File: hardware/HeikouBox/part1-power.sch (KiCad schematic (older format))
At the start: 20 parts, among them J101 5V, U101 LD1117S33TR, U102 LD1117S25TR, U103 LD1117S12TR

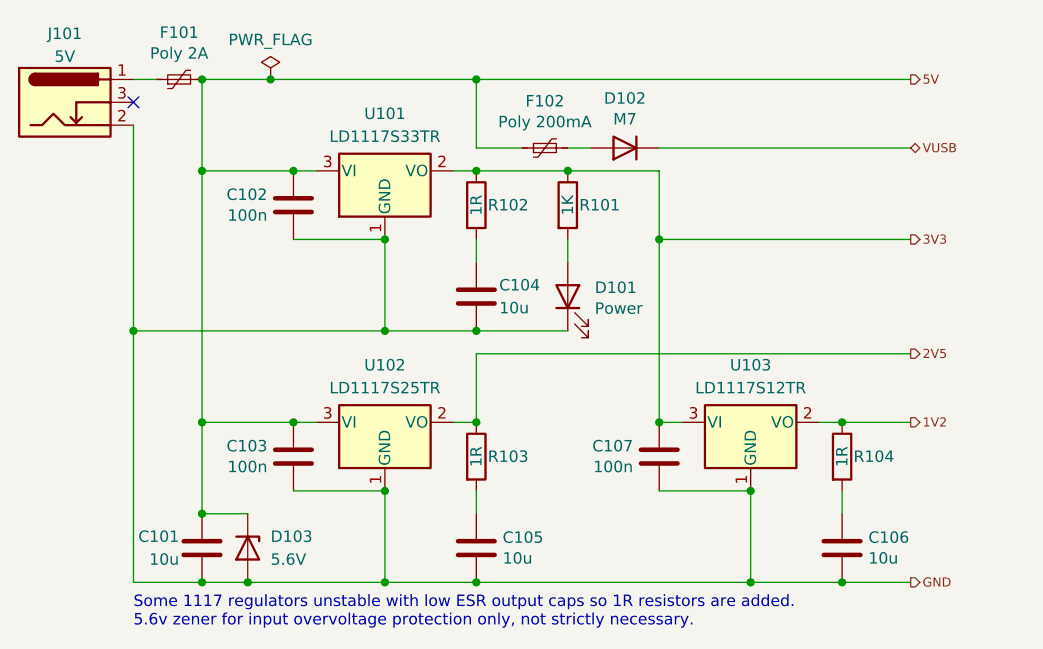
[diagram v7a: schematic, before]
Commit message: Update regulator capacitor values
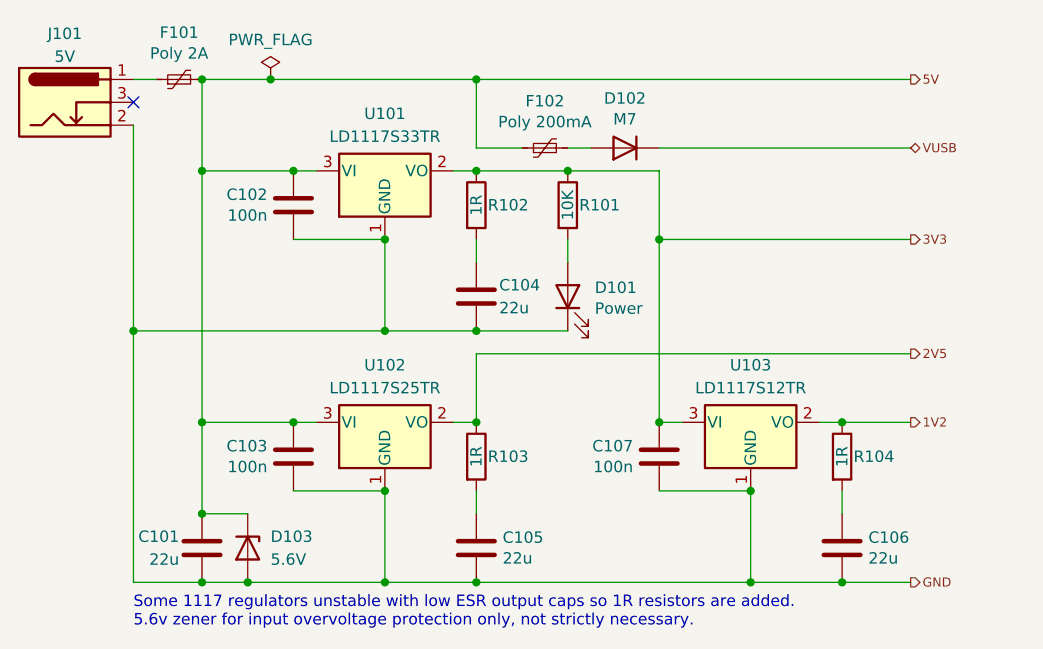
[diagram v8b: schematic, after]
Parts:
- C101, C104, C105, C106: value 10u -> 22u
- R101: value 1K -> 10K
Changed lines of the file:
@@
 	4200 2600 4200 2700
-$Comp
-L Device:R R?
-U 1 1 63836B0F
-P 2600 2450
-AR Path="/63836B0F" Ref="R?"  Part="1"
-AR Path="/644CBAED/63836B0F" Ref="R103"  Part="1"
-AR Path="/729F86A7/63836B0F" Ref="R?"  Part="1"
-F 0 "R103" H 2650 2450 50  0000 L CNN
-F 1 "1R" V 2600 2450 50  0000 C CNN
-F 2 "Resistor_SMD:R_0805_2012Metric_Pad1.20x1.40mm_HandSolder" V 2530 2450 50  0001 C CNN
-F 3 "~" H 2600 2450 50  0001 C CNN
-	1    2600 2450
-	1    0    0    -1
-$EndComp
 $Comp
 L Device:C C?
@@
 AR Path="/729F86A7/67C00E15" Ref="C?"  Part="1"
 F 0 "C106" H 4315 2896 50  0000 L CNN
-F 1 "10u" H 4315 2805 50  0000 L CNN
+F 1 "22u" H 4315 2805 50  0000 L CNN
 F 2 "Capacitor_SMD:C_0805_2012Metric_Pad1.18x1.45mm_HandSolder" H 4238 2700 50  0001 C CNN
 F 3 "~" H 4200 2850 50  0001 C CNN
@@
 AR Path="/729F86A7/67C00DA5" Ref="R?"  Part="1"
 F 0 "R101" H 3050 1350 50  0000 L CNN
-F 1 "1K" V 3000 1350 50  0000 C CNN
+F 1 "10K" V 3000 1350 50  0000 C CNN
 F 2 "Resistor_SMD:R_0603_1608Metric_Pad0.98x0.95mm_HandSolder" V 2930 1350 50  0001 C CNN
 F 3 "~" H 3000 1350 50  0001 C CNN
@@
 AR Path="/729F86A7/67C00E04" Ref="C?"  Part="1"
 F 0 "C105" H 2715 2896 50  0000 L CNN
-F 1 "10u" H 2715 2805 50  0000 L CNN
+F 1 "22u" H 2715 2805 50  0000 L CNN
 F 2 "Capacitor_SMD:C_0805_2012Metric_Pad1.18x1.45mm_HandSolder" H 2638 2700 50  0001 C CNN
 F 3 "~" H 2600 2850 50  0001 C CNN
@@
 AR Path="/729F86A7/67C00DAB" Ref="C?"  Part="1"
 F 0 "C104" H 2700 1800 50  0000 L CNN
-F 1 "10u" H 2700 1700 50  0000 L CNN
+F 1 "22u" H 2700 1700 50  0000 L CNN
 F 2 "Capacitor_SMD:C_0805_2012Metric_Pad1.18x1.45mm_HandSolder" H 2638 1600 50  0001 C CNN
 F 3 "~" H 2600 1750 50  0001 C CNN
@@
 AR Path="/729F86A7/67C00DB6" Ref="C?"  Part="1"
 F 0 "C101" H 1300 2900 50  0000 R CNN
-F 1 "10u" H 1300 2800 50  0000 R CNN
+F 1 "22u" H 1300 2800 50  0000 R CNN
 F 2 "Capacitor_SMD:C_0805_2012Metric_Pad1.18x1.45mm_HandSolder" H 1438 2700 50  0001 C CNN
 F 3 "~" H 1400 2850 50  0001 C CNN
@@
 Wire Wire Line
 	3400 1500 3400 1200
+$Comp
+L Device:R R?
+U 1 1 63836B0F
+P 2600 2450
+AR Path="/63836B0F" Ref="R?"  Part="1"
+AR Path="/644CBAED/63836B0F" Ref="R103"  Part="1"
+AR Path="/729F86A7/63836B0F" Ref="R?"  Part="1"
+F 0 "R103" H 2650 2450 50  0000 L CNN
+F 1 "1R" V 2600 2450 50  0000 C CNN
+F 2 "Resistor_SMD:R_0805_2012Metric_Pad1.20x1.40mm_HandSolder" V 2530 2450 50  0001 C CNN
+F 3 "~" H 2600 2450 50  0001 C CNN
+	1    2600 2450
+	1    0    0    -1
+$EndComp
 $EndSCHEMATC
